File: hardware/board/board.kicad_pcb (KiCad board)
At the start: 2 copper layers, 100 x 30 mm, 41 parts, among them J1 DC THRU, J2 DC THRU, J3 DC OUT, J4 DC IN, J5 DC IN, J6 DC OUT, J7 Eurorack Power, J8 Eurorack Power, SW1 ON/OFF, U1 VX7805-500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

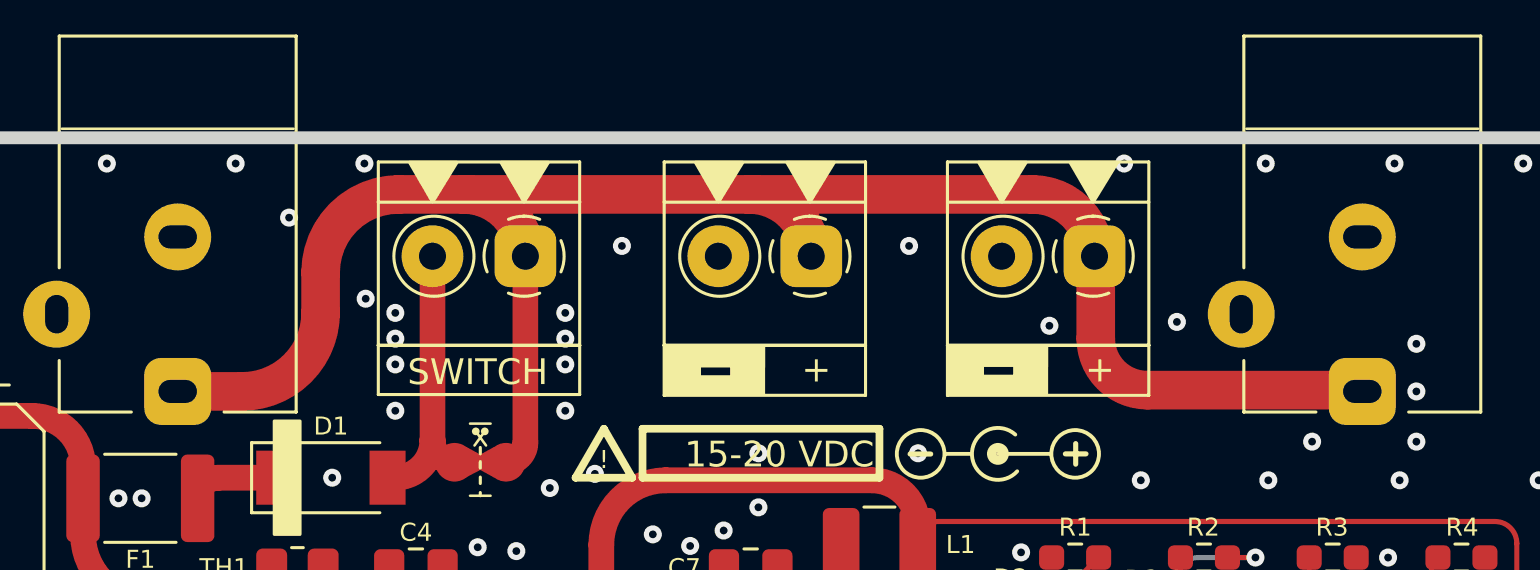
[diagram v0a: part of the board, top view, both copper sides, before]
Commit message: Widen some traces- again
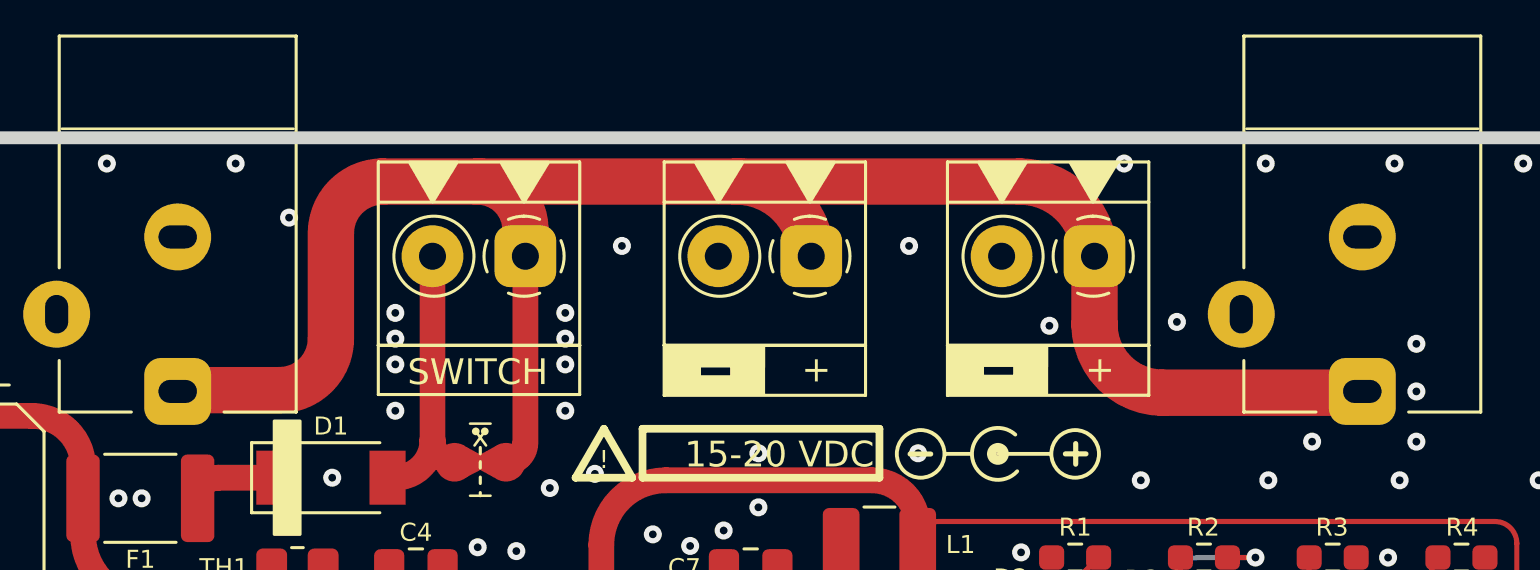
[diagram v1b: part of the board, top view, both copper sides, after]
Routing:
- net +VDC: track 78.1 -> 74.9 mm
- net GND: vias 167 -> 165
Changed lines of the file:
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@@
   (via (at 138.5 114.975) (size 0.7) (drill 0.3) (layers "F.Cu" "B.Cu") (free) (net 1))
   (via (at 112.05 100.225) (size 0.7) (drill 0.3) (layers "F.Cu" "B.Cu") (free) (net 1))
-  (via (at 80.5 94.075) (size 0.7) (drill 0.3) (layers "F.Cu" "B.Cu") (free) (net 1))
   (via (at 61.7 106.375) (size 0.7) (drill 0.3) (layers "F.Cu" "B.Cu") (free) (net 1))
   (via (at 84.9 113.575) (size 0.7) (drill 0.3) (layers "F.Cu" "B.Cu") (free) (net 1))
@@
   (via (at 88.3 100.875) (size 0.7) (drill 0.3) (layers "F.Cu" "B.Cu") (free) (net 1))
   (via (at 121.35 104.875) (size 0.7) (drill 0.3) (layers "F.Cu" "B.Cu") (free) (net 1))
-  (via (at 80.55 99.325) (size 0.7) (drill 0.3) (layers "F.Cu" "B.Cu") (free) (net 1))
   (via (at 87.975 112.25) (size 0.7) (drill 0.3) (layers "F.Cu" "B.Cu") (free) (net 1))
   (via (at 148.3 104.275) (size 0.7) (drill 0.3) (layers "F.Cu" "B.Cu") (free) (net 1))
@@
   (arc (start 100.54 115.04) (mid 100.257358 114.357642) (end 99.575 114.075) (width 1) (layer "F.Cu") (net 7))
   (segment (start 107.00455 111.382951) (end 109.0125 109.375) (width 0.2) (layer "F.Cu") (net 8))
-  (segment (start 84.7 95.275) (end 95.4508 95.275) (width 1.5) (layer "F.Cu") (net 9))
-  (segment (start 108.9 100.875) (end 108.9 97.7242) (width 1.5) (layer "F.Cu") (net 9))
-  (segment (start 95.4508 95.275) (end 106.4508 95.275) (width 1.5) (layer "F.Cu") (net 9))
-  (segment (start 84.7 95.275) (end 81.825 95.275) (width 1) (layer "F.Cu") (net 9))
+  (segment (start 108.8508 97.675) (end 108.8508 100.3258) (width 1.8) (layer "F.Cu") (net 9))
+  (segment (start 79.2 96.775) (end 79.2 100.875) (width 1.8) (layer "F.Cu") (net 9))
+  (segment (start 77.2 102.875) (end 73.3 102.875) (width 1.8) (layer "F.Cu") (net 9))
+  (segment (start 94.9508 94.775) (end 105.9508 94.775) (width 1.8) (layer "F.Cu") (net 9))
+  (segment (start 84.9 94.775) (end 94.9508 94.775) (width 1.8) (layer "F.Cu") (net 9))
+  (segment (start 86.7508 97.675) (end 86.7508 96.6258) (width 1.8) (layer "F.Cu") (net 9))
   (segment (start 86.7508 97.675) (end 86.7508 97.3258) (width 1) (layer "F.Cu") (net 9))
-  (segment (start 73.25 102.925) (end 75.75 102.925) (width 1.5) (layer "F.Cu") (net 9))
-  (segment (start 119.2 102.875) (end 110.9 102.875) (width 1.5) (layer "F.Cu") (net 9))
+  (segment (start 84.9 94.775) (end 81.2 94.775) (width 1.8) (layer "F.Cu") (net 9))
   (segment (start 86.7508 97.675) (end 86.7508 104.9242) (width 1) (layer "F.Cu") (net 9))
-  (segment (start 78.8 99.875) (end 78.8 98.3) (width 1.5) (layer "F.Cu") (net 9))
-  (segment (start 81.825 95.275) (end 84.3508 95.275) (width 1.5) (layer "F.Cu") (net 9))
-  (arc (start 95.4508 95.275) (mid 97.147856 95.977944) (end 97.8508 97.675) (width 1.5) (layer "F.Cu") (net 9))
+  (segment (start 111.5 102.975) (end 119.2 102.975) (width 1.8) (layer "F.Cu") (net 9))
   (arc (start 86.7508 104.9242) (mid 86.530896 105.455096) (end 86 105.675) (width 1) (layer "F.Cu") (net 9))
-  (arc (start 84.3508 95.275) (mid 86.047856 95.977944) (end 86.7508 97.675) (width 1.5) (layer "F.Cu") (net 9))
-  (arc (start 119.25 102.925) (mid 119.235355 102.889645) (end 119.2 102.875) (width 1.5) (layer "F.Cu") (net 9))
-  (arc (start 86.7508 97.3258) (mid 86.150135 95.875665) (end 84.7 95.275) (width 1) (layer "F.Cu") (net 9))
-  (arc (start 110.9 102.875) (mid 109.485786 102.289214) (end 108.9 100.875) (width 1.5) (layer "F.Cu") (net 9))
-  (arc (start 75.75 102.925) (mid 77.906676 102.031676) (end 78.8 99.875) (width 1.5) (layer "F.Cu") (net 9))
-  (arc (start 78.8 98.3) (mid 79.686002 96.161002) (end 81.825 95.275) (width 1.5) (layer "F.Cu") (net 9))
-  (arc (start 106.4508 95.275) (mid 108.147856 95.977944) (end 108.8508 97.675) (width 1.5) (layer "F.Cu") (net 9))
-  (arc (start 108.9 97.7242) (mid 108.88559 97.68941) (end 108.8508 97.675) (width 1.5) (layer "F.Cu") (net 9))
+  (arc (start 79.2 100.875) (mid 78.614214 102.289214) (end 77.2 102.875) (width 1.8) (layer "F.Cu") (net 9))
+  (arc (start 108.8508 100.3258) (mid 109.626733 102.199067) (end 111.5 102.975) (width 1.8) (layer "F.Cu") (net 9))
+  (arc (start 73.3 102.875) (mid 73.264645 102.889645) (end 73.25 102.925) (width 1.8) (layer "F.Cu") (net 9))
+  (arc (start 94.9508 94.775) (mid 97.00141 95.62439) (end 97.8508 97.675) (width 1.8) (layer "F.Cu") (net 9))
+  (arc (start 81.2 94.775) (mid 79.785786 95.360786) (end 79.2 96.775) (width 1.8) (layer "F.Cu") (net 9))
+  (arc (start 119.2 102.975) (mid 119.235355 102.960355) (end 119.25 102.925) (width 1.8) (layer "F.Cu") (net 9))
+  (arc (start 86.7508 96.6258) (mid 86.208713 95.317087) (end 84.9 94.775) (width 1.8) (layer "F.Cu") (net 9))
+  (arc (start 105.9508 94.775) (mid 108.00141 95.62439) (end 108.8508 97.675) (width 1.8) (layer "F.Cu") (net 9))
   (segment (start 76.9 109.725) (end 76.9 109.975) (width 1) (layer "F.Cu") (net 10))
   (segment (start 100.2 106.375) (end 92.2 106.375) (width 1) (layer "F.Cu") (net 10))

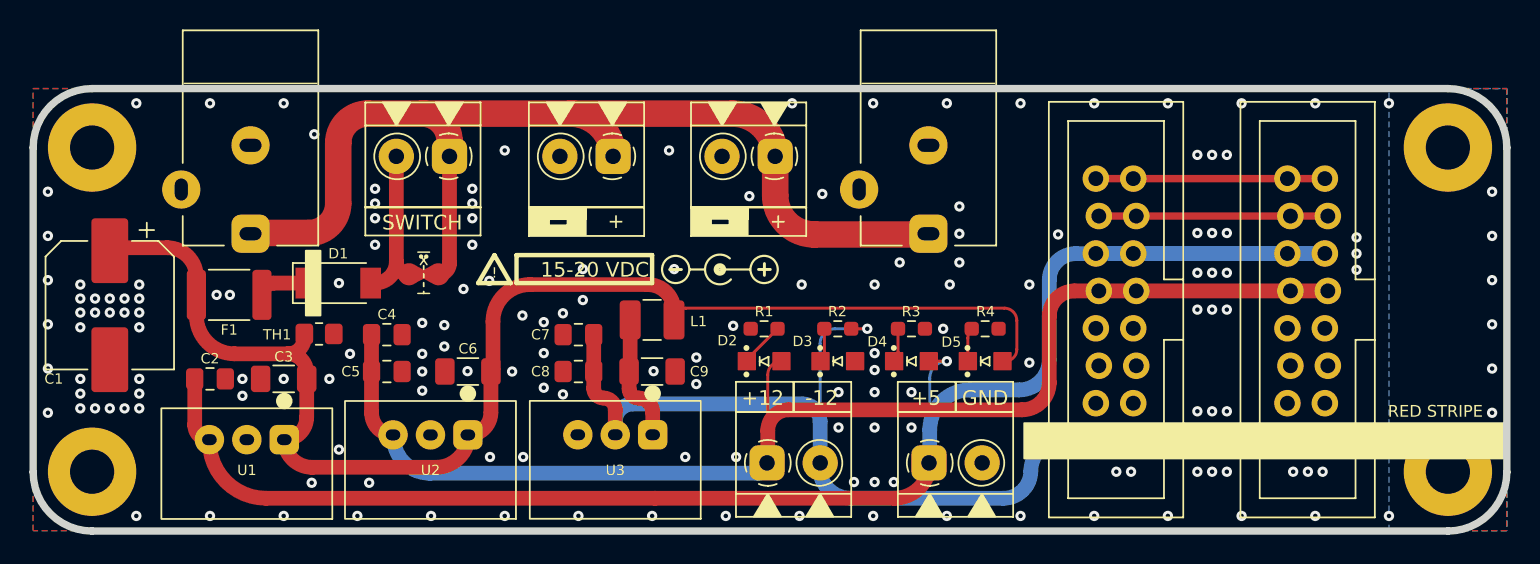
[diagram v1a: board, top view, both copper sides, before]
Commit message: hardware: various updates (v4)
- switched to winterbloom footprints for caps and resistors
- use fancytext labels
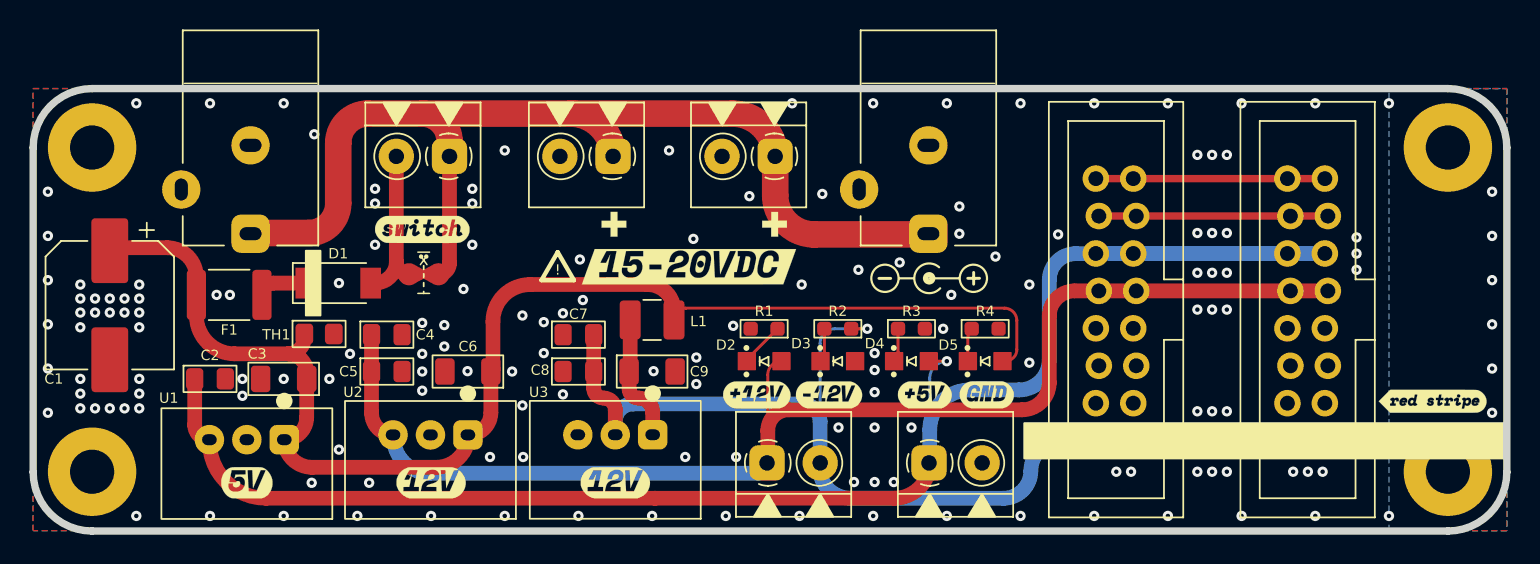
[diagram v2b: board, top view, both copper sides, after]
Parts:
- added G***: LOGO, LOGO, F.Cu at (153.6, 114.5)
- added G***: LOGO, LOGO, F.Cu at (84.9, 102.8)
- added G***: LOGO, LOGO, F.Cu at (119.0, 114.0)
- added G***: LOGO, LOGO, F.Cu at (107.6, 114.0)
- added G***: LOGO, LOGO, F.Cu at (97.9, 102.3)
- added G***: LOGO, LOGO, B.Cu at (84.2, 104.2)
- added G***: LOGO, LOGO, F.Cu at (108.8, 102.3)
- added G***: LOGO, LOGO, F.Cu at (98.0, 120.0)
- added G***: LOGO, LOGO, F.Cu at (103.0, 105.4)
- added G***: LOGO, LOGO, F.Cu at (73.0, 120.0)
- added G***: LOGO, LOGO, F.Cu at (112.5, 114.0)
- added G***: LOGO, LOGO, F.Cu at (123.2, 114.0)
- added G***: LOGO, LOGO, F.Cu at (85.5, 120.0)
- added G***: LOGO, LOGO, F.Cu at (154.5, 104.7)
- C2, C4, C5, C7, C8: footprint Capacitor_SMD:C_0805_2012Metric_Pad1.18x1.45mm_HandSolder -> winterbloom:C_0805_HandSolder
- C3, C6, C9: footprint Capacitor_SMD:C_1206_3216Metric_Pad1.33x1.80mm_HandSolder -> winterbloom:C_1206_HandSolder
- R1, R2, R3, R4: footprint Resistor_SMD:R_0603_1608Metric_Pad0.98x0.95mm_HandSolder -> winterbloom:R_0603_HandSolder
- TH1: footprint Resistor_SMD:R_0805_2012Metric_Pad1.20x1.40mm_HandSolder -> winterbloom:R_0805_HandSolder
- moved POLARITY 14.2 mm to (119.3, 105.9)
- moved WNTR 0.10 mm to (105.5, 108.1)
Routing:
- net GND: vias 165 -> 160
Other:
- board text added: "${REVISION} ${ISSUE_DATE} ${COMMENT2} ${COMMENT3}"
- board text removed: "${TITLE} ${REVISION} ${ISSUE_DATE} ${COMMENT2} ${COMMENT3}"
- board text removed: "+"
- board text removed: "+12"
- board text removed: "+5"
- board text removed: "-12"
- board text removed: "15-20 VDC"
- board text removed: "GND"
- board text removed: "RED STRIPE"
- board text removed: "SWITCH"
- board text removed: "TRANS RIGHTS"
